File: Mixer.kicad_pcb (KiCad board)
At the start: 2 copper layers, 60 x 100 mm, 48 parts, among them J1 Audio-Jack-2_Switch, J2 Conn_02x05_Odd_Even, J3 Audio-Jack-2_Switch, J4 Audio-Jack-2_Switch, J5 Audio-Jack-2_Switch, J6 Audio-Jack-2_Switch, J7 Audio-Jack-2_Switch, U1 TL074

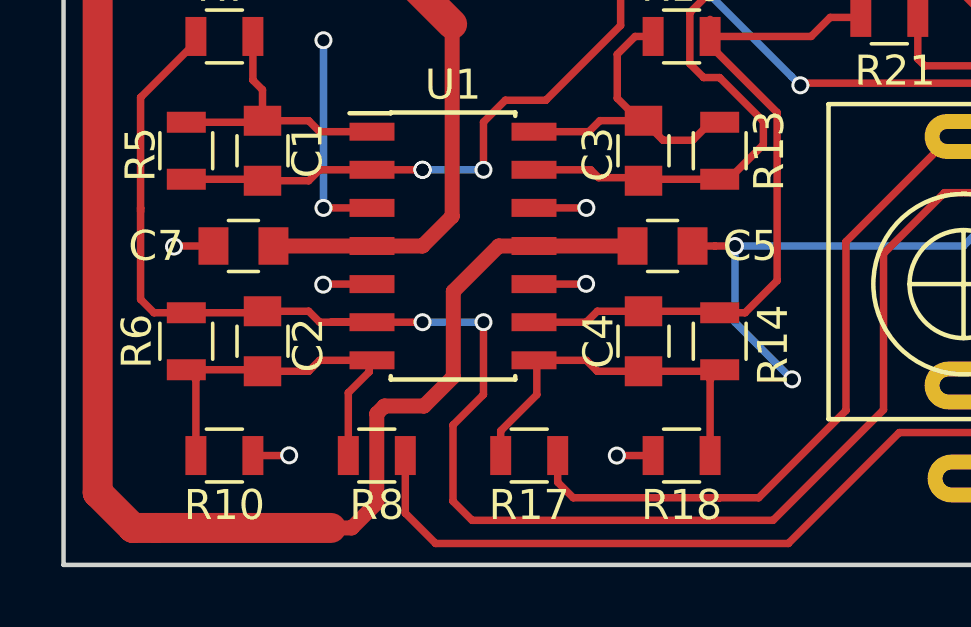
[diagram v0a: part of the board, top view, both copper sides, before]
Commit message: Corrected power pins for TL074, now Rev B.
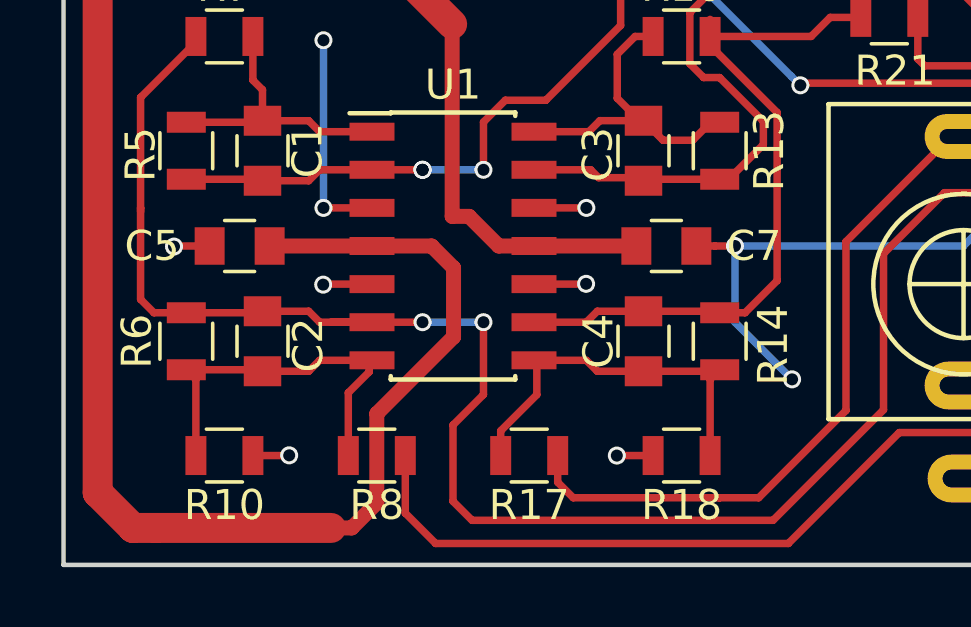
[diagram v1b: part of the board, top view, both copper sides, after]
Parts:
- moved C7 14.1 mm to (86.6, 133.3), turned to 180 degrees
- moved C5 14.1 mm to (72.4, 133.3), turned to 180 degrees
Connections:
- U1 pad 11: +12VA -> -12VA
- U1 pad 4: -12VA -> +12VA
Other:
- board text added: "Modular Mixer, Rev B"
- board text removed: "Modular Mixer, Rev A"
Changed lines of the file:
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@@
     (links 95)
     (no_connects 0)
-    (area 47.955716 40.539999 131.620001 154.680001)
+    (area 66.444999 43.904999 126.595001 144.055001)
     (thickness 1.6)
     (drawings 16)
-    (tracks 411)
+    (tracks 410)
     (zones 0)
     (modules 48)
@@
   )
   (setup
-    (last_trace_width 0.25)
+    (last_trace_width 0.5)
     (user_trace_width 0.25)
     (user_trace_width 0.5)
@@
       (net 10 GND))
     (pad 4 smd rect (at -2.7 0) (size 1.5 0.6) (layers F.Cu F.Paste F.Mask)
-      (net 11 -12VA))
+      (net 9 +12VA))
     (pad 5 smd rect (at -2.7 1.27) (size 1.5 0.6) (layers F.Cu F.Paste F.Mask)
       (net 10 GND))
@@
       (net 10 GND))
     (pad 11 smd rect (at 2.7 0) (size 1.5 0.6) (layers F.Cu F.Paste F.Mask)
-      (net 9 +12VA))
+      (net 11 -12VA))
     (pad 12 smd rect (at 2.7 -1.27) (size 1.5 0.6) (layers F.Cu F.Paste F.Mask)
       (net 10 GND))
@@
   )
   (module Capacitors_SMD:C_0805 (layer F.Cu)
-    (at 72.517 133.35)
+    (at 86.614 133.35 180)
     (descr "Capacitor SMD 0805, reflow soldering, AVX (see smccp.pdf)")
     (tags "capacitor 0805")
     (attr smd)
-    (fp_text reference C7 (at -2.921 0) (layer F.SilkS)
-      (effects (font (size 1 1) (thickness 0.15)))
-    )
-    (fp_text value 100n (at 0 1.75) (layer F.Fab)
-      (effects (font (size 1 1) (thickness 0.15)))
-    )
-    (fp_text user %R (at 0 -1.5) (layer F.Fab)
+    (fp_text reference C7 (at -2.921 0 180) (layer F.SilkS)
+      (effects (font (size 1 1) (thickness 0.15)))
+    )
+    (fp_text value 100n (at 0 1.75 180) (layer F.Fab)
+      (effects (font (size 1 1) (thickness 0.15)))
+    )
+    (fp_text user %R (at 0 -1.5 180) (layer F.Fab)
       (effects (font (size 1 1) (thickness 0.15)))
     )
@@
     (fp_line (start 1.75 0.87) (end 1.75 -0.88) (layer F.CrtYd) (width 0.05))
     (fp_line (start 1.75 0.87) (end -1.75 0.87) (layer F.CrtYd) (width 0.05))
-    (pad 1 smd rect (at -1 0) (size 1 1.25) (layers F.Cu F.Paste F.Mask)
-      (net 10 GND))
-    (pad 2 smd rect (at 1 0) (size 1 1.25) (layers F.Cu F.Paste F.Mask)
+    (pad 1 smd rect (at -1 0 180) (size 1 1.25) (layers F.Cu F.Paste F.Mask)
+      (net 10 GND))
+    (pad 2 smd rect (at 1 0 180) (size 1 1.25) (layers F.Cu F.Paste F.Mask)
       (net 11 -12VA))
     (model Capacitors_SMD.3dshapes/C_0805.wrl
@@
   )
   (module Capacitors_SMD:C_0805 (layer F.Cu)
-    (at 86.487 133.35)
+    (at 72.39 133.35 180)
     (descr "Capacitor SMD 0805, reflow soldering, AVX (see smccp.pdf)")
     (tags "capacitor 0805")
     (attr smd)
-    (fp_text reference C5 (at 2.921 0) (layer F.SilkS)
-      (effects (font (size 1 1) (thickness 0.15)))
-    )
-    (fp_text value 100n (at 0 1.75) (layer F.Fab)
-      (effects (font (size 1 1) (thickness 0.15)))
-    )
-    (fp_text user %R (at 0 -1.5) (layer F.Fab)
+    (fp_text reference C5 (at 2.921 0 180) (layer F.SilkS)
+      (effects (font (size 1 1) (thickness 0.15)))
+    )
+    (fp_text value 100n (at 0 1.75 180) (layer F.Fab)
+      (effects (font (size 1 1) (thickness 0.15)))
+    )
+    (fp_text user %R (at 0 -1.5 180) (layer F.Fab)
       (effects (font (size 1 1) (thickness 0.15)))
     )
@@
     (fp_line (start 1.75 0.87) (end 1.75 -0.88) (layer F.CrtYd) (width 0.05))
     (fp_line (start 1.75 0.87) (end -1.75 0.87) (layer F.CrtYd) (width 0.05))
-    (pad 1 smd rect (at -1 0) (size 1 1.25) (layers F.Cu F.Paste F.Mask)
+    (pad 1 smd rect (at -1 0 180) (size 1 1.25) (layers F.Cu F.Paste F.Mask)
       (net 9 +12VA))
-    (pad 2 smd rect (at 1 0) (size 1 1.25) (layers F.Cu F.Paste F.Mask)
+    (pad 2 smd rect (at 1 0 180) (size 1 1.25) (layers F.Cu F.Paste F.Mask)
       (net 10 GND))
     (model Capacitors_SMD.3dshapes/C_0805.wrl
@@
     (effects (font (size 1.5 1.5) (thickness 0.3)) (justify mirror))
   )
-  (gr_text "Modular Mixer, Rev A" (at 112.52 45.98) (layer B.SilkS)
+  (gr_text "Modular Mixer, Rev B\n" (at 112.52 45.98) (layer B.SilkS)
     (effects (font (size 1.5 1.5) (thickness 0.3)) (justify mirror))
   )
@@
   (segment (start 85.852 135.525) (end 88.342 135.525) (width 0.25) (layer F.Cu) (net 8))
   (segment (start 88.342 135.525) (end 88.392 135.575) (width 0.25) (layer F.Cu) (net 8))
+  (segment (start 76.802 133.35) (end 73.39 133.35) (width 0.5) (layer F.Cu) (net 9))
+  (segment (start 76.802 133.35) (end 78.79 133.35) (width 0.5) (layer F.Cu) (net 9))
+  (segment (start 78.79 133.35) (end 79.52 134.08) (width 0.5) (layer F.Cu) (net 9))
+  (segment (start 79.52 134.08) (end 79.52 136.38) (width 0.5) (layer F.Cu) (net 9))
+  (segment (start 79.52 136.38) (end 76.962 138.938) (width 0.5) (layer F.Cu) (net 9))
+  (segment (start 76.12769 142.748) (end 75.438 142.748) (width 0.5) (layer F.Cu) (net 9))
+  (segment (start 76.962 138.938) (end 76.962 141.91369) (width 0.5) (layer F.Cu) (net 9))
+  (segment (start 76.962 141.91369) (end 76.12769 142.748) (width 0.5) (layer F.Cu) (net 9))
   (segment (start 70.485 61.065) (end 69.11 61.065) (width 1) (layer F.Cu) (net 9))
   (segment (start 69.11 61.065) (end 67.657371 62.517629) (width 1) (layer F.Cu) (net 9))
@@
   (segment (start 68.834 142.748) (end 69.596 142.748) (width 1) (layer F.Cu) (net 9))
   (segment (start 69.596 142.748) (end 75.438 142.748) (width 1) (layer F.Cu) (net 9))
-  (segment (start 82.202 133.35) (end 81.026 133.35) (width 0.5) (layer F.Cu) (net 9))
-  (segment (start 81.026 133.35) (end 79.511856 134.864144) (width 0.5) (layer F.Cu) (net 9))
-  (segment (start 79.511856 134.864144) (end 79.511856 137.708944) (width 0.5) (layer F.Cu) (net 9))
-  (segment (start 76.962 141.91369) (end 76.12769 142.748) (width 0.5) (layer F.Cu) (net 9))
-  (segment (start 79.511856 137.708944) (end 78.5368 138.684) (width 0.5) (layer F.Cu) (net 9))
-  (segment (start 76.962 138.938) (end 76.962 141.91369) (width 0.5) (layer F.Cu) (net 9))
-  (segment (start 78.5368 138.684) (end 77.216 138.684) (width 0.5) (layer F.Cu) (net 9))
-  (segment (start 77.216 138.684) (end 76.962 138.938) (width 0.5) (layer F.Cu) (net 9))
-  (segment (start 76.12769 142.748) (end 75.438 142.748) (width 0.5) (layer F.Cu) (net 9))
-  (segment (start 85.487 133.35) (end 82.202 133.35) (width 0.5) (layer F.Cu) (net 9))
   (segment (start 69.215 54.19) (end 69.215 57.15) (width 1) (layer F.Cu) (net 9))
   (segment (start 70.485 58.42) (end 70.485 61.065) (width 1) (layer F.Cu) (net 9))
@@
   (segment (start 72.832 140.335) (end 74.033748 140.335) (width 0.25) (layer F.Cu) (net 10))
   (via (at 74.041266 140.327482) (size 0.6) (drill 0.4) (layers F.Cu B.Cu) (net 10))
+  (segment (start 82.202 133.35) (end 85.614 133.35) (width 0.5) (layer F.Cu) (net 11))
+  (segment (start 79.474017 132.361983) (end 80.037983 132.361983) (width 0.5) (layer F.Cu) (net 11))
+  (segment (start 80.037983 132.361983) (end 81.026 133.35) (width 0.5) (layer F.Cu) (net 11))
+  (segment (start 82.202 133.35) (end 81.026 133.35) (width 0.5) (layer F.Cu) (net 11))
   (segment (start 69.636234 75.159896) (end 69.596493 75.199637) (width 1) (layer F.Cu) (net 11))
   (segment (start 69.596493 75.199637) (end 71.148703 75.199637) (width 1) (layer F.Cu) (net 11))
@@
   (segment (start 77.343 123.825) (end 79.474017 125.956017) (width 1) (layer F.Cu) (net 11))
   (segment (start 79.474017 125.956017) (end 79.474017 132.361983) (width 0.5) (layer F.Cu) (net 11))
-  (segment (start 79.474017 132.361983) (end 78.486 133.35) (width 0.5) (layer F.Cu) (net 11))
-  (segment (start 78.486 133.35) (end 76.802 133.35) (width 0.5) (layer F.Cu) (net 11))
-  (segment (start 73.517 133.35) (end 76.802 133.35) (width 0.5) (layer F.Cu) (net 11))
   (segment (start 84.074 49.022) (end 83.947 48.895) (width 1) (layer F.Cu) (net 12))
   (segment (start 83.947 48.895) (end 80.645 48.895) (width 1) (layer F.Cu) (net 12))

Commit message: This is revision B of the board.
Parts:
- C1, C2, C3, C4, C5, C7: footprint Capacitors_SMD:C_0805 -> Capacitor_SMD:C_0805_2012Metric; moved to B.Cu
- C6, C8: footprint Capacitors_SMD:CP_Elec_4x5.8 -> Capacitor_SMD:CP_Elec_4x5.8; moved to B.Cu
- D1, D2: footprint Diodes_SMD:D_PowerDI-123 -> Diode_SMD:D_PowerDI-123; moved to B.Cu
- J1, J3, J4, J5, J6: value Audio-Jack-2_Switch -> AudioJack2_Ground_Switch; footprint DTD:PJ398SM -> Local:PJ398SM
- J2: value Conn_02x05_Odd_Even -> AudioJack2_Ground_Switch; footprint Pin_Headers:Pin_Header_Straight_2x05_Pitch2.54mm -> Local:PJ398SM; moved to F.Cu
- J7: value Audio-Jack-2_Switch -> Conn_02x05_Odd_Even; footprint DTD:PJ398SM -> Connector_PinHeader_2.54mm:PinHeader_2x05_P2.54mm_Vertical; moved to B.Cu
- R1, R10, R11, R12, R13, R14, R15, R16, R17, R18, R19, R2, R20, R21, R22, R3, R4, R5, R6, R7, R8, R9: footprint Resistors_SMD:R_0805 -> Resistor_SMD:R_0805_2012Metric; moved to B.Cu
- RV1, RV2, RV3, RV4, RV5, RV6, RV7, RV8: value 47k -> 50k; footprint Potentiometers:Potentiometer_Alps_RK09K_Horizontal -> Local:AlpsRK09K
- U1: footprint Housings_SOIC:SOIC-14_3.9x8.7mm_Pitch1.27mm -> Package_SO:SOIC-14_3.9x8.7mm_P1.27mm; moved to B.Cu
- moved J6 68.9 mm to (139.2, 142.2)
- moved J7 68.6 mm to (106.2, 66.7)
- moved J5 64.4 mm to (118.9, 142.2)
- moved RV4 57.1 mm to (139.2, 121.9), turned to 0 degrees
- moved RV2 45.0 mm to (139.2, 81.3), turned to 0 degrees
- moved D1 44.8 mm to (109.3, 74.3)
- moved RV5 40.6 mm to (118.9, 61.0), turned to 0 degrees
- moved R11 38.4 mm to (136.7, 113.7), turned to 180 degrees
- moved R2 38.4 mm to (136.7, 73.0), turned to 180 degrees
- moved R4 38.4 mm to (136.7, 93.3), turned to 180 degrees
- moved C6 38.4 mm to (95.4, 92.1), turned to 0 degrees
- moved R15 38.4 mm to (136.7, 133.3), turned to 180 degrees
- moved C5 37.9 mm to (110.0, 137.8), turned to 90 degrees
- moved D2 35.9 mm to (105.5, 74.3)
- moved J3 35.8 mm to (98.6, 101.6)
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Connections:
- J7 pad 1: Net-(J7-Pad1) -> Net-(D1-Pad2)
- J7 pad 2: GND -> Net-(D1-Pad2)
- J7 pad 3: Net-(J7-Pad3) -> GND
- R1 pad 2: Net-(J1-Pad1) -> Net-(J1-PadT)
- R11 pad 2: Net-(J5-Pad1) -> Net-(J3-PadT)
- R12 pad 2: Net-(J6-Pad1) -> Net-(J4-PadT)
- R15 pad 2: Net-(J6-Pad1) -> Net-(J4-PadT)
- R17 pad 1: Net-(J7-Pad1) -> Net-(J6-PadT)
- R2 pad 2: Net-(J1-Pad1) -> Net-(J1-PadT)
- R3 pad 2: Net-(J3-Pad1) -> Net-(J2-PadT)
- R4 pad 2: Net-(J3-Pad1) -> Net-(J2-PadT)
- R8 pad 1: Net-(J4-Pad1) -> Net-(J5-PadT)
- R9 pad 2: Net-(J5-Pad1) -> Net-(J3-PadT)
- RV1 pad 1: Net-(R19-Pad2) -> Net-(C3-Pad2)
- RV1 pad 2: Net-(R1-Pad1) -> Net-(R2-Pad1)
- RV1 pad 3: Net-(C1-Pad2) -> Net-(R21-Pad2)
- RV2 pad 1: Net-(R21-Pad2) -> Net-(C3-Pad2)
- RV2 pad 2: Net-(R2-Pad1) -> Net-(R4-Pad1)
- RV2 pad 3: Net-(C3-Pad2) -> Net-(R21-Pad2)
- RV3 pad 1: Net-(R19-Pad2) -> Net-(C3-Pad2)
- RV3 pad 2: Net-(R3-Pad1) -> Net-(R11-Pad1)
- RV3 pad 3: Net-(C1-Pad2) -> Net-(R21-Pad2)
- RV4 pad 1: Net-(R21-Pad2) -> Net-(C3-Pad2)
- RV4 pad 2: Net-(R4-Pad1) -> Net-(R15-Pad1)
- RV4 pad 3: Net-(C3-Pad2) -> Net-(R21-Pad2)
- RV5 pad 1: Net-(R19-Pad2) -> Net-(C1-Pad2)
- RV5 pad 2: Net-(R9-Pad1) -> Net-(R1-Pad1)
- RV5 pad 3: Net-(C1-Pad2) -> Net-(R19-Pad2)
- RV6 pad 1: Net-(R21-Pad2) -> Net-(C1-Pad2)
- RV6 pad 2: Net-(R11-Pad1) -> Net-(R3-Pad1)
- RV6 pad 3: Net-(C3-Pad2) -> Net-(R19-Pad2)
- RV7 pad 1: Net-(R19-Pad2) -> Net-(C1-Pad2)
- RV7 pad 2: Net-(R12-Pad1) -> Net-(R9-Pad1)
- RV7 pad 3: Net-(C1-Pad2) -> Net-(R19-Pad2)
- RV8 pad 1: Net-(R21-Pad2) -> Net-(C1-Pad2)
- RV8 pad 2: Net-(R15-Pad1) -> Net-(R12-Pad1)
- RV8 pad 3: Net-(C3-Pad2) -> Net-(R19-Pad2)
- U1 pad 1: Net-(C1-Pad1) -> Net-(C3-Pad1)
- U1 pad 13: Net-(C3-Pad2) -> Net-(C1-Pad2)
- U1 pad 14: Net-(C3-Pad1) -> Net-(C1-Pad1)
- U1 pad 2: Net-(C1-Pad2) -> Net-(C3-Pad2)
- U1 pad 6: Net-(C2-Pad2) -> Net-(C4-Pad2)
- U1 pad 7: Net-(C2-Pad1) -> Net-(C4-Pad1)
- U1 pad 8: Net-(C4-Pad1) -> Net-(C2-Pad1)
- U1 pad 9: Net-(C4-Pad2) -> Net-(C2-Pad2)
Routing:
- net Net-(J2-PadT): track 0.00 -> 66.8 mm, vias 0 -> 3
- net Net-(J1-Pad1): track 64.8 -> 0.00 mm
- net Net-(J1-PadT): track 0.00 -> 60.8 mm
- net Net-(J4-PadT): track 0.00 -> 53.1 mm, vias 0 -> 2
- net Net-(J3-PadT): track 0.00 -> 51.2 mm, vias 0 -> 2
- net Net-(J3-Pad1): track 47.1 -> 0.00 mm, vias 2 -> 0
- net Net-(J4-Pad1): track 46.9 -> 0.00 mm
- net Net-(J6-Pad1): track 46.7 -> 0.00 mm, vias 2 -> 0
- net Net-(J5-Pad1): track 45.8 -> 0.00 mm, vias 2 -> 0
- net Net-(C2-Pad2): track 67.7 -> 32.3 mm
- net Net-(J5-PadT): track 0.00 -> 33.5 mm
- net Net-(J6-PadT): track 0.00 -> 32.9 mm
- net +12VA: track 115.3 -> 88.2 mm
- net Net-(C4-Pad2): track 23.6 -> 50.6 mm
- net Net-(J7-Pad1): track 22.9 -> 0.00 mm
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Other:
- board size 60 x 100 mm -> 59.9 x 100 mm
- net class Default: clearance 0.2 -> 0.254; trace_width 0.25 -> 0.254; via_dia 0.6 -> 0.8
- rule trace_clearance: 0.2 -> 0.254
- board text added: "Mixer / Attenuverter"
- board text added: "Rev B"
- board text removed: "+12"
- board text removed: "-12"
- board text removed: "Modular Mixer, Rev B"
